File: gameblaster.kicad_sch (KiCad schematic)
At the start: 74 parts, among them IC1 TEA2025, IC10 74LS125, IC12 74LS74, IC2 SAA1099, IC3 SAA1099, IC4 74LS245, IC5 74LS374, IC6 74LS138, IC7 74LS138, IC8 74LS32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

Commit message: Fix some shit
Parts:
- added R14: 1K, gameblaster:RESA400, symbol Device:R_Small_US
- C1, C11: value 0.22uF 16V -> 10uF 16V
- C17, C23: value 1uF tant -> 10uF tant
- C24, C36: value 680pF -> 1000pF
- C25, C26: value 680pF -> 2200pF
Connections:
- net GND: now also R14.2
- net VCC: no longer R19.1
- net VDDA: now also R19.1
- net at C3.1, IC1.14 (BOOT1): no longer C4.2, C5.1
- net at C3.2, IC1.15 (OUT1): now also C4.2, C5.1
- net at C6.2, IC1.2 (OUT2): now also C8.1, C9.1
- net at C6.1, IC1.3 (BOOT2): no longer C8.1, C9.1
- net at IC10.6, IC12.10 (~{S}): now also R14.1
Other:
- note added: "+5V is low for a TEA2025B, but apparently still in operating range. (The Sound Blaster used a 12V -> 9V regulator, but the Game Blaster just uses one of the bus 5V lines for all the analog power.)"
- note removed: "+5V is low for a TEA2025B, but apparently still in operating range. (The Sound Blaster used a 12V -> 9V regulator, but the Game Blaster just used this zener-regulated 12V -> 5V circuit for all the analog power)"
- note removed: "Hey, look! It's a 23.417KHz RC low-pass filter!"
- moved on the sheet: C4

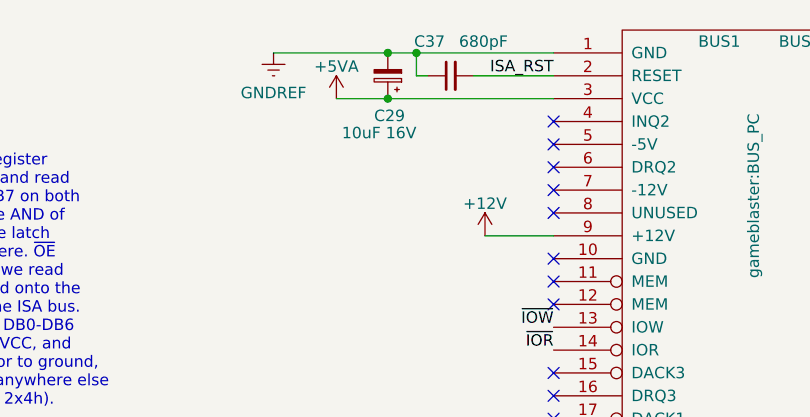
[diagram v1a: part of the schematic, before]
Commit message: Add 3D models for Bracket and Volume pot/knob, update gerbers
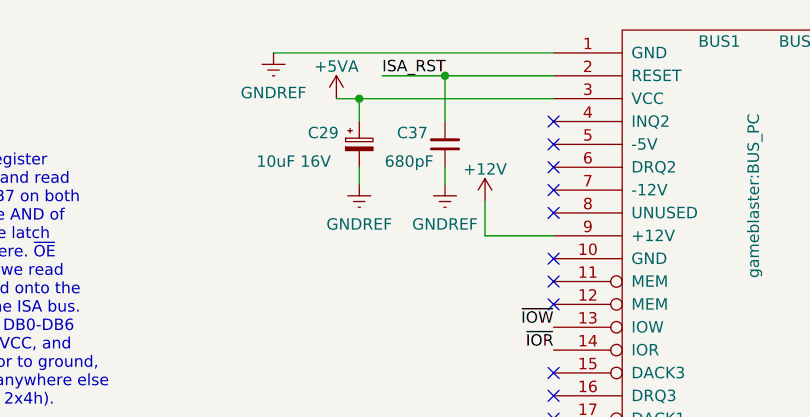
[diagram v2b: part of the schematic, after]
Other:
- moved on the sheet: C29, C37
